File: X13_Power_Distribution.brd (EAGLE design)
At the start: 152.4 x 73.7 mm, 35 parts

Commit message: am sleepy
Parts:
- removed BACKPLANE_GND, BACKPLANE_PWR: (no value), SparkFun-Connectors:2X10
- removed D4: 30V, SparkFun-DiscreteSemi:SOD-323
- added BACKPLANE_GND_1, BACKPLANE_GND_2, BACKPLANE_PWR_1, BACKPLANE_PWR_2: (no value), SparkFun-Connectors:2X10
- BRICK1_VOUT(+), BRICK1_VOUT(-), BRICK2_VOUT(+), BRICK2_VOUT(-): device SparkFun-Connectors:2X5 -> SparkFun-Connectors:2X8
- D6: value 30V -> 20V
- R4, R6, R7: value 1k -> 10k
- moved BRICK1_VOUT(+) 107.0 mm to (-63.2, -53.1)
- moved BRICK1_VOUT(-) 96.2 mm to (-63.2, -46.2)
- moved BRICK2_VOUT(-) 94.5 mm to (-63.2, -39.4)
- moved BRICK2_VOUT(+) 90.3 mm to (-63.2, -32.5)
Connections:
- removed net +48V_RAW: 48V_TETHER.1, 48V_TETHER.3, 48V_TETHER.5, 48V_TETHER.7, 48V_TETHER.9, D6.C
- removed net 3.3V: R4.2, R6.2, R7.2
- removed net C2/PGOOD: BACKPLANE_SMBUS.8, BRICK1_SMBUS.1, BRICK2_SMBUS.1
- removed net N$3: D4.A, R3.2, U$6.1
- removed net N$4: U$6.3
- new net C2_1: BACKPLANE_SMBUS.8, BRICK1_SMBUS.1
- new net C2_2: BACKPLANE_SMBUS.10, BRICK2_SMBUS.1
- new net GND_RAW: 48V_TETHER.10, 48V_TETHER.2, 48V_TETHER.4, 48V_TETHER.6, 48V_TETHER.8, R3.1, U$6.2
- net +12V: now also BACKPLANE_PWR_1.1, BACKPLANE_PWR_1.10, BACKPLANE_PWR_1.11, BACKPLANE_PWR_1.12, BACKPLANE_PWR_1.13, BACKPLANE_PWR_1.14, BACKPLANE_PWR_1.15, BACKPLANE_PWR_1.16, BACKPLANE_PWR_1.17, BACKPLANE_PWR_1.18, BACKPLANE_PWR_1.19, BACKPLANE_PWR_1.2, BACKPLANE_PWR_1.20, BACKPLANE_PWR_1.3, BACKPLANE_PWR_1.4, BACKPLANE_PWR_1.5, BACKPLANE_PWR_1.6, BACKPLANE_PWR_1.7, BACKPLANE_PWR_1.8, BACKPLANE_PWR_1.9, BACKPLANE_PWR_2.1, BACKPLANE_PWR_2.10, BACKPLANE_PWR_2.11, BACKPLANE_PWR_2.12, BACKPLANE_PWR_2.13, BACKPLANE_PWR_2.14, BACKPLANE_PWR_2.15, BACKPLANE_PWR_2.16, BACKPLANE_PWR_2.17, BACKPLANE_PWR_2.18, BACKPLANE_PWR_2.19, BACKPLANE_PWR_2.2, BACKPLANE_PWR_2.20, BACKPLANE_PWR_2.3, BACKPLANE_PWR_2.4, BACKPLANE_PWR_2.5, BACKPLANE_PWR_2.6, BACKPLANE_PWR_2.7, BACKPLANE_PWR_2.8, BACKPLANE_PWR_2.9, BRICK1_VOUT(+).11, BRICK1_VOUT(+).12, BRICK1_VOUT(+).13, BRICK1_VOUT(+).14, BRICK1_VOUT(+).15, BRICK1_VOUT(+).16, BRICK2_VOUT(+).11, BRICK2_VOUT(+).12, BRICK2_VOUT(+).13, BRICK2_VOUT(+).14, BRICK2_VOUT(+).15, BRICK2_VOUT(+).16; no longer BACKPLANE_PWR.1, BACKPLANE_PWR.10, BACKPLANE_PWR.11, BACKPLANE_PWR.12, BACKPLANE_PWR.13, BACKPLANE_PWR.14, BACKPLANE_PWR.15, BACKPLANE_PWR.16, BACKPLANE_PWR.17, BACKPLANE_PWR.18, BACKPLANE_PWR.19, BACKPLANE_PWR.2, BACKPLANE_PWR.20, BACKPLANE_PWR.3, BACKPLANE_PWR.4, BACKPLANE_PWR.5, BACKPLANE_PWR.6, BACKPLANE_PWR.7, BACKPLANE_PWR.8, BACKPLANE_PWR.9
- net +3.3V: now also BACKPLANE_SMBUS.9, R4.2, R6.2, R7.2; no longer BACKPLANE_SMBUS.10
- net +48V: now also 48V_TETHER.1, 48V_TETHER.3, 48V_TETHER.5, 48V_TETHER.7, 48V_TETHER.9, D6.C
- net +5V: now also CONVERSION_R.1, CONVERSION_R.2; no longer BACKPLANE_SMBUS.9, CONVERSION_L.3, CONVERSION_L.4
- net 12V_GND: now also BACKPLANE_GND_1.1, BACKPLANE_GND_1.10, BACKPLANE_GND_1.11, BACKPLANE_GND_1.12, BACKPLANE_GND_1.13, BACKPLANE_GND_1.14, BACKPLANE_GND_1.15, BACKPLANE_GND_1.16, BACKPLANE_GND_1.17, BACKPLANE_GND_1.18, BACKPLANE_GND_1.19, BACKPLANE_GND_1.2, BACKPLANE_GND_1.20, BACKPLANE_GND_1.3, BACKPLANE_GND_1.4, BACKPLANE_GND_1.5, BACKPLANE_GND_1.6, BACKPLANE_GND_1.7, BACKPLANE_GND_1.8, BACKPLANE_GND_1.9, BACKPLANE_GND_2.1, BACKPLANE_GND_2.10, BACKPLANE_GND_2.11, BACKPLANE_GND_2.12, BACKPLANE_GND_2.13, BACKPLANE_GND_2.14, BACKPLANE_GND_2.15, BACKPLANE_GND_2.16, BACKPLANE_GND_2.17, BACKPLANE_GND_2.18, BACKPLANE_GND_2.19, BACKPLANE_GND_2.2, BACKPLANE_GND_2.20, BACKPLANE_GND_2.3, BACKPLANE_GND_2.4, BACKPLANE_GND_2.5, BACKPLANE_GND_2.6, BACKPLANE_GND_2.7, BACKPLANE_GND_2.8, BACKPLANE_GND_2.9, BRICK1_VOUT(-).11, BRICK1_VOUT(-).12, BRICK1_VOUT(-).13, BRICK1_VOUT(-).14, BRICK1_VOUT(-).15, BRICK1_VOUT(-).16, BRICK2_VOUT(-).11, BRICK2_VOUT(-).12, BRICK2_VOUT(-).13, BRICK2_VOUT(-).14, BRICK2_VOUT(-).15, BRICK2_VOUT(-).16; no longer BACKPLANE_GND.1, BACKPLANE_GND.10, BACKPLANE_GND.11, BACKPLANE_GND.12, BACKPLANE_GND.13, BACKPLANE_GND.14, BACKPLANE_GND.15, BACKPLANE_GND.16, BACKPLANE_GND.17, BACKPLANE_GND.18, BACKPLANE_GND.19, BACKPLANE_GND.2, BACKPLANE_GND.20, BACKPLANE_GND.3, BACKPLANE_GND.4, BACKPLANE_GND.5, BACKPLANE_GND.6, BACKPLANE_GND.7, BACKPLANE_GND.8, BACKPLANE_GND.9
- net 48V_GND: now also CONVERSION_L.3, CONVERSION_L.4, U$6.3; no longer 48V_TETHER.10, 48V_TETHER.2, 48V_TETHER.4, 48V_TETHER.6, 48V_TETHER.8, CONVERSION_R.1, CONVERSION_R.2
- net GND: no longer R3.1, U$6.2
- net N$5: now also R3.2, U$6.1; no longer D4.C

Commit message: It's pretty now :3
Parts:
- removed J3, J4: (no value), SparkFun-Connectors:BANANA_CONN
- added 48V_POE: POE_TERMINAL, Dist_POE:CONN2_282834-2_TEC
- 48V_TETHER: value (none) -> DIST_TO_TETHER; device SparkFun-Connectors:2X5 -> Dist_To_Tether_Connector:CON6_P5MM_VER_TERM-BLK_TYC
- D6: value 20V -> 15V
- moved 48V_TETHER 98.4 mm to (-60.7, -66.3)
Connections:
- removed net N$5: D6.A, R3.2, U$6.1
- new net 48_GND: U$6.2
- new net N$3: D6.C, R3.1, U$6.1
- net +12V: no longer BRICK1_VOUT(+).1, BRICK1_VOUT(+).10, BRICK1_VOUT(+).11, BRICK1_VOUT(+).12, BRICK1_VOUT(+).13, BRICK1_VOUT(+).14, BRICK1_VOUT(+).15, BRICK1_VOUT(+).16, BRICK1_VOUT(+).2, BRICK1_VOUT(+).3, BRICK1_VOUT(+).4, BRICK1_VOUT(+).5, BRICK1_VOUT(+).6, BRICK1_VOUT(+).7, BRICK1_VOUT(+).8, BRICK1_VOUT(+).9, BRICK2_VOUT(+).1, BRICK2_VOUT(+).10, BRICK2_VOUT(+).11, BRICK2_VOUT(+).12, BRICK2_VOUT(+).13, BRICK2_VOUT(+).14, BRICK2_VOUT(+).15, BRICK2_VOUT(+).16, BRICK2_VOUT(+).2, BRICK2_VOUT(+).3, BRICK2_VOUT(+).4, BRICK2_VOUT(+).5, BRICK2_VOUT(+).6, BRICK2_VOUT(+).7, BRICK2_VOUT(+).8, BRICK2_VOUT(+).9
- net +12V_A: now also BRICK1_VOUT(+).1, BRICK1_VOUT(+).10, BRICK1_VOUT(+).11, BRICK1_VOUT(+).12, BRICK1_VOUT(+).13, BRICK1_VOUT(+).14, BRICK1_VOUT(+).15, BRICK1_VOUT(+).16, BRICK1_VOUT(+).2, BRICK1_VOUT(+).3, BRICK1_VOUT(+).4, BRICK1_VOUT(+).5, BRICK1_VOUT(+).6, BRICK1_VOUT(+).7, BRICK1_VOUT(+).8, BRICK1_VOUT(+).9
- net +12V_B: now also BRICK2_VOUT(+).1, BRICK2_VOUT(+).10, BRICK2_VOUT(+).11, BRICK2_VOUT(+).12, BRICK2_VOUT(+).13, BRICK2_VOUT(+).14, BRICK2_VOUT(+).15, BRICK2_VOUT(+).16, BRICK2_VOUT(+).2, BRICK2_VOUT(+).3, BRICK2_VOUT(+).4, BRICK2_VOUT(+).5, BRICK2_VOUT(+).6, BRICK2_VOUT(+).7, BRICK2_VOUT(+).8, BRICK2_VOUT(+).9
- net +3.3V: now also CONVERSION_R.5; no longer CONVERSION_L.5
- net +48V: now also 48V_POE.1, 48V_TETHER.2, CONVERSION_L.5, R3.2; no longer 48V_TETHER.5, 48V_TETHER.7, 48V_TETHER.9, CONVERSION_R.5, D6.C, J3.P$1
- net 48V_GND: now also 48V_POE.2; no longer J4.P$1, U$6.3
- net GND_RAW: now also 48V_TETHER.5, D6.A, U$6.3; no longer 48V_TETHER.10, 48V_TETHER.2, 48V_TETHER.8, R3.1, U$6.2

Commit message: layout!
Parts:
- removed BACKPLANE_SMBUS: (no value), SparkFun-Connectors:2X5
- removed U$3: NMOSFET-DPAK, MotherboardParts:DPAK
- added C1, C2, C3: (no value), capacitor-wima:C2.5-4
- added Q1: 310mA/60V/1.6Ω, SparkFun-DiscreteSemi:SOT323
- added U1, U2: Value, Dist_OR_Controller:DGK0008A_N
- CONVERSION_L: device SparkFun-Connectors:1X05 -> SparkFun-Connectors:1X04
- CONVERSION_R: device SparkFun-Connectors:1X05 -> SparkFun-Connectors:2X4
- D2: device diode:SOT23 -> SparkFun-DiscreteSemi:SOD-323
- U$1, U$2: value DIODE -> IRF1018EPBF; device DIODE:DIODE -> Reverse_Voltage_NMOS:TO263
- moved BRICK2_VOUT(+) 179.4 mm to (99.8, 42.2), turned to 90 degrees
- moved BRICK2_VOUT(-) 171.3 mm to (99.1, 15.5), turned to 90 degrees
- moved 48V_TETHER 166.6 mm to (43.7, 63.5)
- moved BRICK2_VIN(+) 162.4 mm to (109.0, 42.2), turned to 90 degrees
- moved CONVERSION_L 161.6 mm to (108.2, 58.4), turned to 90 degrees
- moved BACKPLANE_GND_1 157.7 mm to (94.2, 4.06)
- moved CONVERSION_R 143.8 mm to (118.4, 61.0), turned to 90 degrees
- moved BRICK2_VIN(-) 138.0 mm to (109.0, 23.1), turned to 90 degrees
- moved BRICK1_VOUT(+) 137.2 mm to (13.5, 60.7), turned to 270 degrees
- moved D2 133.7 mm to (67.3, 36.8), turned to 180 degrees
- moved BACKPLANE_GND_2 132.8 mm to (67.6, 4.06)
- moved U$2 131.8 mm to (81.8, 20.6), turned to 90 degrees
- moved BRICK2_SMBUS 129.4 mm to (89.9, 54.6), turned to 90 degrees
- moved R2 117.0 mm to (67.6, 49.3), turned to 90 degrees
- moved R3 111.9 mm to (58.4, 48.5), turned to 90 degrees
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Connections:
- removed net 48_GND: U$6.2
- new net 5V_GND: CONVERSION_R.5, CONVERSION_R.6, CONVERSION_R.7, CONVERSION_R.8
- new net N$10: U$1.1, U1.2, U1.6
- new net N$13: U$2.1, U2.2, U2.6
- new net N$5: C2.1, U2.7
- new net N$6: C2.2, U2.1
- new net N$7: C1.2, U1.1
- new net N$9: C1.1, U1.7
- net +12V: now also C3.1, U$1.3, U$2.3, U1.8, U2.8; no longer U$1.OUT, U$2.OUT
- net +12V_A: now also U$1.2, U1.4; no longer U$1.IN1, U$1.IN2
- net +12V_B: now also U$2.2, U2.4; no longer U$2.IN1, U$2.IN2
- net +3.3V: now also CONVERSION_R.3; no longer BACKPLANE_SMBUS.9, CONVERSION_R.5
- net +48V: now also CONVERSION_L.3, CONVERSION_L.4; no longer CONVERSION_L.5
- net +5V: no longer BACKPLANE_SMBUS.1, BACKPLANE_SMBUS.3, BACKPLANE_SMBUS.5, BACKPLANE_SMBUS.7, CONVERSION_R.3
- net 12V_GND: now also C3.2
- net 48V_GND: now also D2.A, Q1.2, U$6.2; no longer CONVERSION_L.3, CONVERSION_L.4, D2.1, U$3.3
- net ALERT: no longer BACKPLANE_SMBUS.4
- net C2_1: no longer BACKPLANE_SMBUS.8
- net C2_2: no longer BACKPLANE_SMBUS.10
- net CLK: no longer BACKPLANE_SMBUS.6
- net DATA: no longer BACKPLANE_SMBUS.2
- net N$2: now also Q1.1; no longer U$3.1
- net ON/OFF: now also D2.C, Q1.3; no longer D2.3, U$3.4

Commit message: Design review time
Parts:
- removed 48V_TETHER: DIST_TO_TETHER, Dist_To_Tether_Connector:CON6_P5MM_VER_TERM-BLK_TYC
- added BACKPLANE_SIMBUS: 2X6 FEMALE, SparkFun-Connectors:2X6
- added TETHER: 48V, Dist_To_Tether_Connector:CON6_P5MM_VER_TERM-BLK_TYC
- moved BRICK1_SMBUS 88.7 mm to (111.8, 40.6)
- moved R6 87.3 mm to (116.8, 49.5), turned to 0 degrees
- moved R4 83.0 mm to (116.8, 53.3), turned to 0 degrees
- moved BACKPLANE_GND_1 82.5 mm to (11.7, 4.06)
- moved R7 80.5 mm to (116.8, 45.7), turned to 0 degrees
- moved R5 45.9 mm to (49.5, 27.9)
- moved D5 45.6 mm to (49.5, 22.9)
- moved CONVERSION_L 42.2 mm to (66.0, 59.7)
- moved BRICK2_SMBUS 37.4 mm to (111.5, 24.1)
- moved BRICK2_VIN(-) 29.1 mm to (99.3, 50.5), turned to 270 degrees
- moved BACKPLANE_GND_2 27.9 mm to (95.5, 4.06)
- moved BRICK1_VOUT(+) 26.7 mm to (13.5, 34.0)
- moved BACKPLANE_PWR_2 26.7 mm to (67.6, 4.06)
- moved BACKPLANE_PWR_1 25.4 mm to (39.6, 4.06)
- moved BRICK2_VIN(+) 20.3 mm to (90.4, 50.5), turned to 270 degrees
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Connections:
- new net ALERT_1: BACKPLANE_SIMBUS.4
- new net ALERT_2: BACKPLANE_SIMBUS.6
- new net N$4: BACKPLANE_SIMBUS.11, BACKPLANE_SIMBUS.9
- net +3.3V: now also BACKPLANE_SIMBUS.7
- net +48V: now also TETHER.1, TETHER.2, TETHER.3; no longer 48V_TETHER.1, 48V_TETHER.2, 48V_TETHER.3
- net +5V: now also BACKPLANE_SIMBUS.1, BACKPLANE_SIMBUS.3, BACKPLANE_SIMBUS.5
- net C2_1: now also BACKPLANE_SIMBUS.10
- net C2_2: now also BACKPLANE_SIMBUS.12
- net CLK: now also BACKPLANE_SIMBUS.8
- net DATA: now also BACKPLANE_SIMBUS.2
- net GND_RAW: now also TETHER.4, TETHER.5, TETHER.6; no longer 48V_TETHER.4, 48V_TETHER.5, 48V_TETHER.6

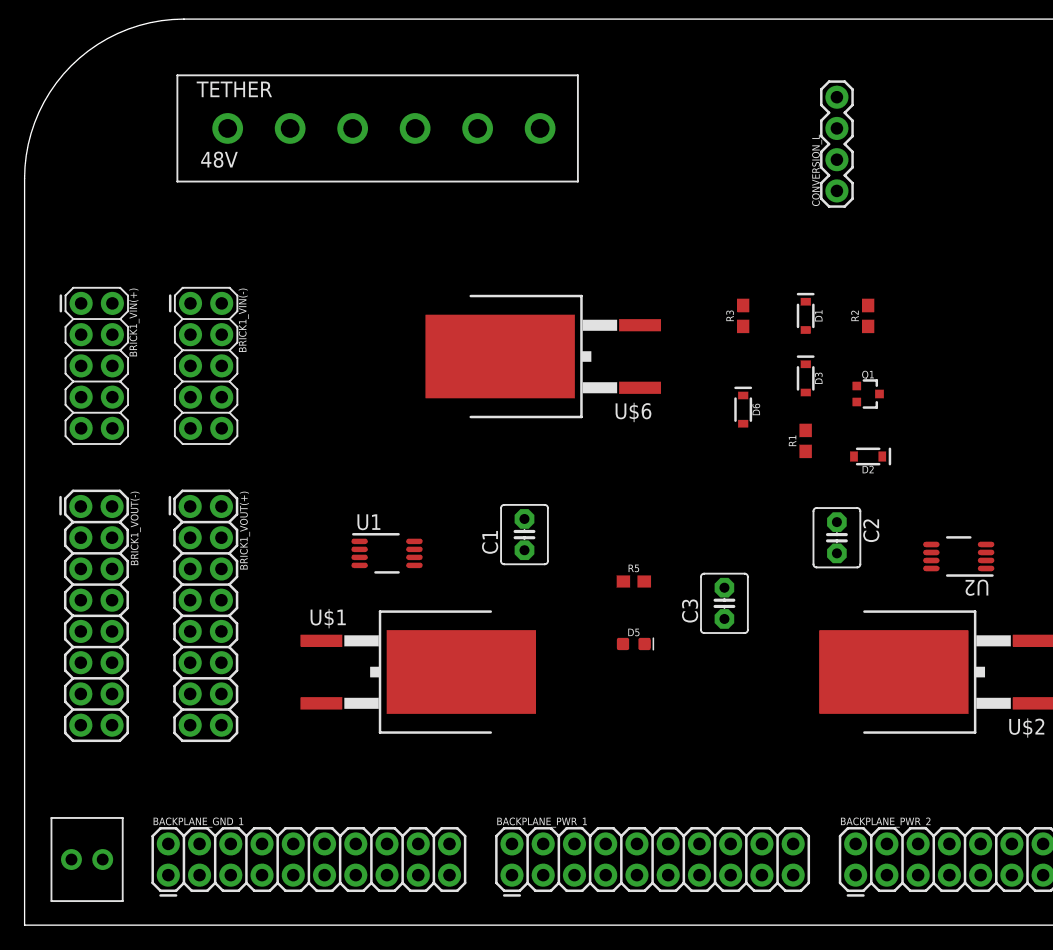
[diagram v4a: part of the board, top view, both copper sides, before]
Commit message: cap placeholders fixed
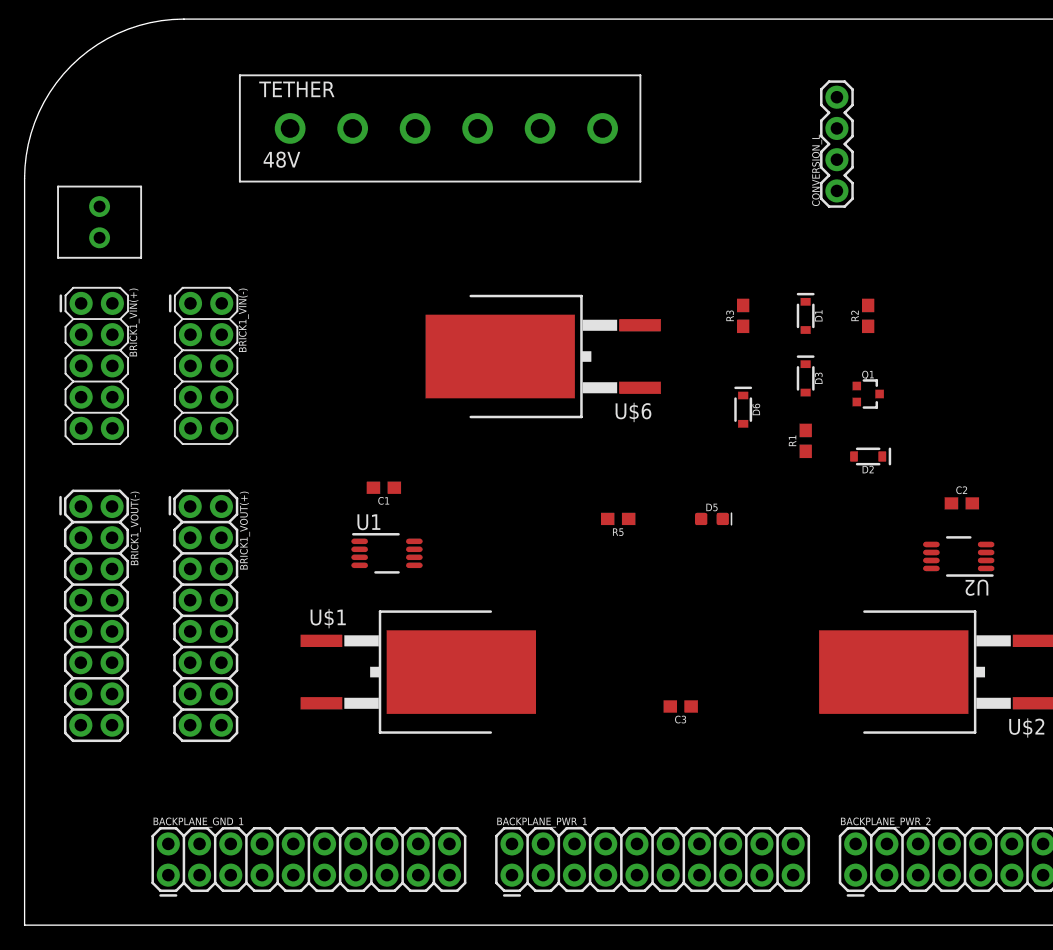
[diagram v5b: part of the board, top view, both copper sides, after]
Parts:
- C1, C2, C3: device capacitor-wima:C2.5-4 -> SparkFun-Capacitors:0603
- moved 48V_POE 50.6 mm to (6.10, 55.9), turned to 90 degrees
- moved C1 12.0 mm to (29.2, 35.6), turned to 180 degrees
- moved D5 12.0 mm to (55.9, 33.0)
- moved C2 10.5 mm to (76.2, 34.3), turned to 0 degrees
- moved C3 9.11 mm to (53.3, 17.8), turned to 180 degrees
- moved R5 5.24 mm to (48.3, 33.0), turned to 180 degrees
- moved TETHER 5.08 mm to (21.6, 64.8)

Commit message: 2020/11/21
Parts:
- C3: value (none) -> 330uF; device SparkFun-Capacitors:0603 -> brick-capacitor-UCM1H331MNL1GS:CAPAE1030X1050N
- moved BRICK1_SMBUS 95.6 mm to (20.3, 12.7), turned to 0 degrees
- moved CONVERSION_L 81.4 mm to (147.3, 54.6), turned to 180 degrees
- moved C3 66.5 mm to (100.3, 64.8)
- moved CONVERSION_R 54.0 mm to (143.5, 16.5), turned to 0 degrees
- moved R4 53.9 mm to (147.3, 8.89)
- moved R7 51.8 mm to (147.3, 3.81)
- moved R6 49.5 mm to (141.0, 6.35)
- moved U$6 36.4 mm to (75.2, 64.0)
- moved U$1 27.7 mm to (58.4, 19.1), flipped to the bottom, turned to 90 degrees
- moved BRICK1_VOUT(+) 25.9 mm to (39.4, 33.0)
- moved BRICK1_VIN(-) 25.9 mm to (39.4, 49.5)
- moved C1 25.4 mm to (54.6, 34.3), flipped to the bottom, turned to 0 degrees
- moved U1 25.2 mm to (54.6, 29.2), flipped to the bottom, turned to 180 degrees
- moved R3 22.2 mm to (80.0, 54.6), turned to 270 degrees
- moved BRICK2_VIN(-) 20.4 mm to (119.6, 49.3)
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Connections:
- net +12V: now also C3.+; no longer C3.1
- net 12V_GND: now also C3.-; no longer C3.2

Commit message: routed :)
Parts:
- removed BACKPLANE_GND_1, BACKPLANE_GND_2, BACKPLANE_PWR_1, BACKPLANE_PWR_2: (no value), SparkFun-Connectors:2X10
- removed BACKPLANE_SIMBUS: 2X6 FEMALE, SparkFun-Connectors:2X6
- removed CONVERSION_L: (no value), SparkFun-Connectors:1X04
- removed CONVERSION_R: (no value), SparkFun-Connectors:2X4
- added 5V_POE: POE_TERMINAL, Dist_POE:CONN2_282834-2_TEC
- added BACKPLANE_LOGIC: IPL1-107-01-L-D-RE-P, Backplane_Dist_Logic_Connector:IPL1-107-01-L-D-RE-P
- added CONVERSION_BOTTOM: (no value), SparkFun-Connectors:2X4
- added CONVERSION_TOP: (no value), SparkFun-Connectors:1X04
- added H1, H2, H3, H4: 6-32-HOLE, Mounting Holes:6-32-HOLE
- added J1: (no value), Samtec MPPT Hermaphoditic 10 pos - MPPT-10-01-01-L-RA-SD:MPPT-10-01-01-L-RA-SD
- added R8: 10k, SparkFun-Resistors:0603
- U1, U2: device Dist_OR_Controller:DGK0008A_N -> Dist_OR_Controller:DGK0008A_M
- moved U$2 49.3 mm to (115.6, 29.2)
- moved D1 48.9 mm to (108.0, 69.8), turned to 180 degrees
- moved D3 46.9 mm to (102.9, 69.8), flipped to the bottom, turned to 0 degrees
- moved BRICK1_SMBUS 45.9 mm to (31.8, 57.1)
- moved U2 45.9 mm to (115.6, 40.6), flipped to the bottom, turned to 0 degrees
- moved C2 45.7 mm to (116.8, 35.6), flipped to the bottom, turned to 180 degrees
- moved R2 45.5 mm to (110.5, 67.3)
- moved R1 45.0 mm to (97.8, 68.6), flipped to the bottom, turned to 180 degrees
- moved BRICK2_VIN(+) 44.2 mm to (134.6, 49.5), turned to 0 degrees
- moved Q1 42.3 mm to (104.1, 66.0), flipped to the bottom, turned to 180 degrees
- moved D2 39.6 mm to (97.8, 64.8), flipped to the bottom, turned to 0 degrees
- moved BRICK2_VIN(-) 36.0 mm to (134.6, 16.5), turned to 0 degrees
- moved D5 35.9 mm to (78.7, 26.7), turned to 0 degrees
- moved BRICK1_VIN(+) 33.0 mm to (7.62, 16.5), turned to 0 degrees
- moved BRICK1_VIN(-) 31.7 mm to (7.62, 49.5), turned to 0 degrees
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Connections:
- removed net ALERT: BRICK1_SMBUS.4, BRICK2_SMBUS.4, R6.1
- removed net N$4: BACKPLANE_SIMBUS.11, BACKPLANE_SIMBUS.9
- net +12V: now also J1.1@1, J1.1@2, J1.1@3, J1.1@4, J1.1@5, J1.1@6, J1.2@1, J1.2@2, J1.2@3, J1.2@4, J1.2@5, J1.2@6, J1.3@1, J1.3@2, J1.3@3, J1.3@4, J1.3@5, J1.3@6, J1.4@1, J1.4@2, J1.4@3, J1.4@4, J1.4@5, J1.4@6, J1.5@1, J1.5@2, J1.5@3, J1.5@4, J1.5@5, J1.5@6; no longer BACKPLANE_PWR_1.1, BACKPLANE_PWR_1.10, BACKPLANE_PWR_1.11, BACKPLANE_PWR_1.12, BACKPLANE_PWR_1.13, BACKPLANE_PWR_1.14, BACKPLANE_PWR_1.15, BACKPLANE_PWR_1.16, BACKPLANE_PWR_1.17, BACKPLANE_PWR_1.18, BACKPLANE_PWR_1.19, BACKPLANE_PWR_1.2, BACKPLANE_PWR_1.20, BACKPLANE_PWR_1.3, BACKPLANE_PWR_1.4, BACKPLANE_PWR_1.5, BACKPLANE_PWR_1.6, BACKPLANE_PWR_1.7, BACKPLANE_PWR_1.8, BACKPLANE_PWR_1.9, BACKPLANE_PWR_2.1, BACKPLANE_PWR_2.10, BACKPLANE_PWR_2.11, BACKPLANE_PWR_2.12, BACKPLANE_PWR_2.13, BACKPLANE_PWR_2.14, BACKPLANE_PWR_2.15, BACKPLANE_PWR_2.16, BACKPLANE_PWR_2.17, BACKPLANE_PWR_2.18, BACKPLANE_PWR_2.19, BACKPLANE_PWR_2.2, BACKPLANE_PWR_2.20, BACKPLANE_PWR_2.3, BACKPLANE_PWR_2.4, BACKPLANE_PWR_2.5, BACKPLANE_PWR_2.6, BACKPLANE_PWR_2.7, BACKPLANE_PWR_2.8, BACKPLANE_PWR_2.9
- net +3.3V: now also BACKPLANE_LOGIC.4, CONVERSION_BOTTOM.3, R8.2; no longer BACKPLANE_SIMBUS.7, CONVERSION_R.3
- net +48V: now also CONVERSION_TOP.3, CONVERSION_TOP.4; no longer CONVERSION_L.3, CONVERSION_L.4
- net +5V: now also 5V_POE.1, BACKPLANE_LOGIC.1, BACKPLANE_LOGIC.2, BACKPLANE_LOGIC.3, CONVERSION_BOTTOM.1, CONVERSION_BOTTOM.2, CONVERSION_BOTTOM.4; no longer BACKPLANE_SIMBUS.1, BACKPLANE_SIMBUS.3, BACKPLANE_SIMBUS.5, CONVERSION_R.1, CONVERSION_R.2, CONVERSION_R.4
- net 12V_GND: now also J1.10@1, J1.10@2, J1.10@3, J1.10@4, J1.10@5, J1.10@6, J1.6@1, J1.6@2, J1.6@3, J1.6@4, J1.6@5, J1.6@6, J1.7@1, J1.7@2, J1.7@3, J1.7@4, J1.7@5, J1.7@6, J1.8@1, J1.8@2, J1.8@3, J1.8@4, J1.8@5, J1.8@6, J1.9@1, J1.9@2, J1.9@3, J1.9@4, J1.9@5, J1.9@6; no longer BACKPLANE_GND_1.1, BACKPLANE_GND_1.10, BACKPLANE_GND_1.11, BACKPLANE_GND_1.12, BACKPLANE_GND_1.13, BACKPLANE_GND_1.14, BACKPLANE_GND_1.15, BACKPLANE_GND_1.16, BACKPLANE_GND_1.17, BACKPLANE_GND_1.18, BACKPLANE_GND_1.19, BACKPLANE_GND_1.2, BACKPLANE_GND_1.20, BACKPLANE_GND_1.3, BACKPLANE_GND_1.4, BACKPLANE_GND_1.5, BACKPLANE_GND_1.6, BACKPLANE_GND_1.7, BACKPLANE_GND_1.8, BACKPLANE_GND_1.9, BACKPLANE_GND_2.1, BACKPLANE_GND_2.10, BACKPLANE_GND_2.11, BACKPLANE_GND_2.12, BACKPLANE_GND_2.13, BACKPLANE_GND_2.14, BACKPLANE_GND_2.15, BACKPLANE_GND_2.16, BACKPLANE_GND_2.17, BACKPLANE_GND_2.18, BACKPLANE_GND_2.19, BACKPLANE_GND_2.2, BACKPLANE_GND_2.20, BACKPLANE_GND_2.3, BACKPLANE_GND_2.4, BACKPLANE_GND_2.5, BACKPLANE_GND_2.6, BACKPLANE_GND_2.7, BACKPLANE_GND_2.8, BACKPLANE_GND_2.9
- net 48V_GND: now also CONVERSION_TOP.1, CONVERSION_TOP.2; no longer CONVERSION_L.1, CONVERSION_L.2
- net 5V_GND: now also 5V_POE.2, BACKPLANE_LOGIC.5, BACKPLANE_LOGIC.6, CONVERSION_BOTTOM.5, CONVERSION_BOTTOM.6, CONVERSION_BOTTOM.7, CONVERSION_BOTTOM.8; no longer CONVERSION_R.5, CONVERSION_R.6, CONVERSION_R.7, CONVERSION_R.8
- net ALERT_1: now also BACKPLANE_LOGIC.11, BRICK1_SMBUS.4, R8.1; no longer BACKPLANE_SIMBUS.4
- net ALERT_2: now also BACKPLANE_LOGIC.10, BRICK2_SMBUS.4, R6.1; no longer BACKPLANE_SIMBUS.6
- net C2_1: now also BACKPLANE_LOGIC.8; no longer BACKPLANE_SIMBUS.10
- net C2_2: now also BACKPLANE_LOGIC.7; no longer BACKPLANE_SIMBUS.12
- net CLK: now also BACKPLANE_LOGIC.9; no longer BACKPLANE_SIMBUS.8
- net DATA: now also BACKPLANE_LOGIC.12; no longer BACKPLANE_SIMBUS.2
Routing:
- net DATA: track 0.00 -> 194.0 mm, vias 0 -> 4
- net CLK: track 0.00 -> 185.2 mm, vias 0 -> 4
- net ALERT_1: track 0.00 -> 174.5 mm, vias 0 -> 5
- net ON/OFF: track 0.00 -> 171.7 mm, vias 0 -> 1
- net 5V_GND: track 0.00 -> 160.1 mm, vias 0 -> 3
- net +3.3V: track 0.00 -> 145.8 mm, vias 0 -> 2
- net +5V: track 0.00 -> 139.0 mm, vias 0 -> 4
- net ALERT_2: track 0.00 -> 104.6 mm, vias 0 -> 3
- net C2_2: track 0.00 -> 102.2 mm, vias 0 -> 2
- net C2_1: track 0.00 -> 62.7 mm, vias 0 -> 1
- net N$13: track 0.00 -> 38.1 mm, vias 0 -> 1
- net +12V: track 0.00 -> 33.8 mm, vias 0 -> 2
- net N$10: track 0.00 -> 25.6 mm
- net +12V_A: track 0.00 -> 18.9 mm, vias 0 -> 3
- net N$3: track 0.00 -> 15.4 mm, vias 0 -> 1
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- added copper zone on layer 1, net +12V
- added copper zone on layer 1, net +12V_A
- added copper zone on layer 1, net +12V_B
- added copper zone on layer 1, net +48V
- added copper zone on layer 16, net +5V
- added copper zone on layer 1, net 12V_GND
- added copper zone on layer 16, net 12V_GND
- added copper zone on layer 16, net 48V_GND
- added copper zone on layer 16, net 5V_GND
- added copper zone on layer 16, net GND_RAW
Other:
- board text added: "+12V"
- board text added: "+12V_A"
- board text added: "+48V"
- board text added: "+5V"
- board text added: "12V_GND"
- board text added: "48V_GND"
